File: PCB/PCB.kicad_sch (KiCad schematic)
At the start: 17 parts, among them J1 Conn_01x06_Female, J2 5054332681, U13 74HC165, U15 LT3042xMSE, U16 74HC165

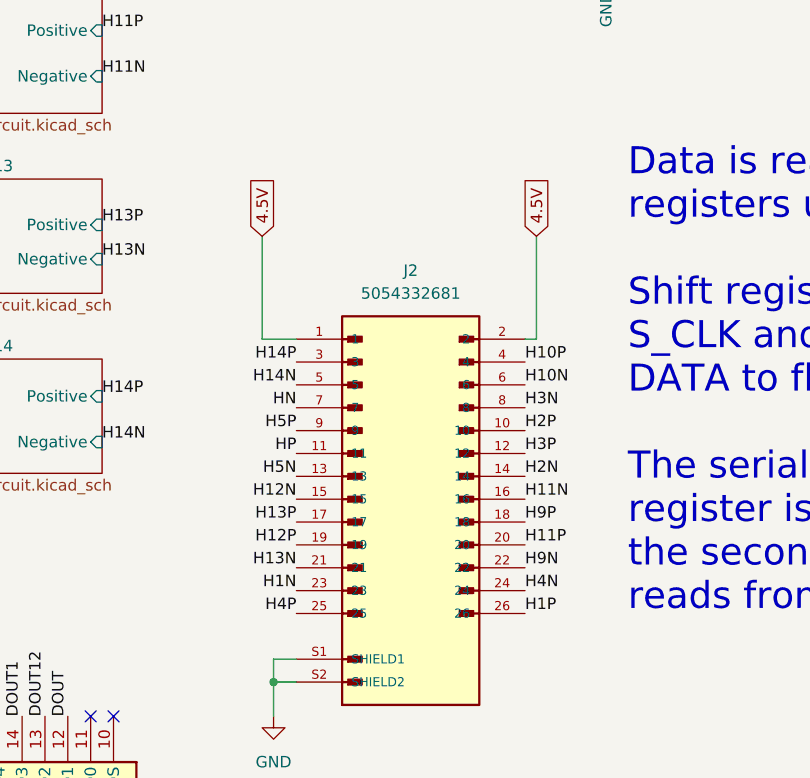
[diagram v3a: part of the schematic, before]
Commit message: New 75 by 75 mm
Dout has been traced, mostly on the same plane and have started on some of the required parts for the individual hx711 and will continue setting up sequential zones to reduce wires.
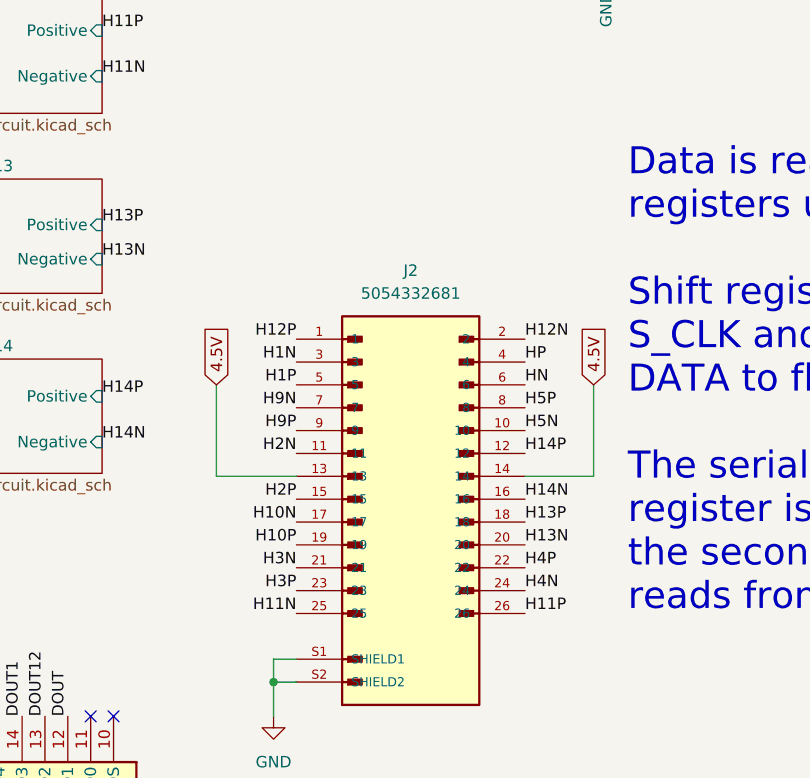
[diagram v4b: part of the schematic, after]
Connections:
- net 4.5V: now also J2.13, J2.14; no longer J2.1, J2.2
- net H10N: now also J2.17; no longer J2.6
- net H10P: now also J2.19; no longer J2.4
- net H11N: now also J2.25; no longer J2.16
- net H11P: now also J2.26; no longer J2.20
- net H12N: now also J2.2; no longer J2.15
- net H12P: now also J2.1; no longer J2.19
- net H13N: now also J2.20; no longer J2.21
- net H13P: now also J2.18; no longer J2.17
- net H14N: now also J2.16; no longer J2.5
- net H14P: now also J2.12; no longer J2.3
- net H1N: now also J2.3; no longer J2.23
- net H1P: now also J2.5; no longer J2.26
- net H2N: now also J2.11; no longer J2.14
- net H2P: now also J2.15; no longer J2.10
- net H3N: now also J2.21; no longer J2.8
- net H3P: now also J2.23; no longer J2.12
- net H4P: now also J2.22; no longer J2.25
- net H5N: now also J2.10; no longer J2.13
- net H5P: now also J2.8; no longer J2.9
- net H9N: now also J2.7; no longer J2.22
- net H9P: now also J2.9; no longer J2.18
- net HN: now also J2.6; no longer J2.7
- net HP: now also J2.4; no longer J2.11

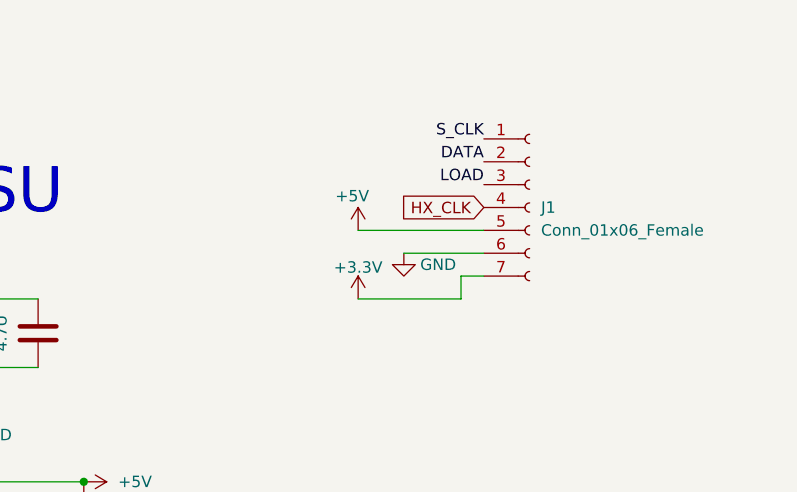
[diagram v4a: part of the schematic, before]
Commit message: Updated 7 pin header pinout
Pinout has been adjusted to match the pinout of the flight computer.
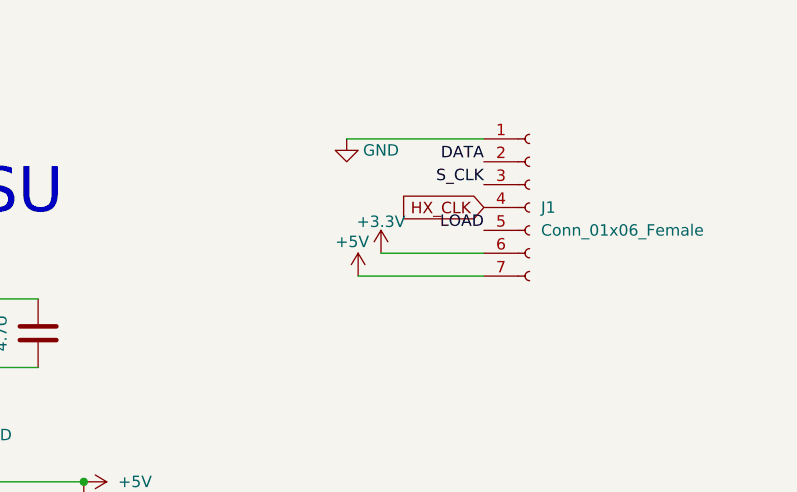
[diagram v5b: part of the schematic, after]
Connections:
- net +3.3V: now also J1.6 (Pin_6); no longer J1.7 (Pin_7)
- net +5V: now also J1.7 (Pin_7); no longer J1.5 (Pin_5)
- net GND: now also J1.1 (Pin_1); no longer J1.6 (Pin_6)
- net LOAD: now also J1.5 (Pin_5); no longer J1.3 (Pin_3)
- net S_CLK: now also J1.3 (Pin_3); no longer J1.1 (Pin_1)
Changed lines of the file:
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@@
 	(wire
 		(pts
-			(xy 251.46 41.91) (xy 248.92 41.91)
+			(xy 168.91 64.77) (xy 168.91 73.66)
 		)
 		(stroke
@@
 	(wire
 		(pts
-			(xy 168.91 64.77) (xy 168.91 73.66)
+			(xy 132.08 158.75) (xy 132.08 161.29)
 		)
 		(stroke
@@
 	(wire
 		(pts
-			(xy 132.08 158.75) (xy 132.08 161.29)
+			(xy 262.89 73.66) (xy 255.27 73.66)
 		)
 		(stroke
@@
 	(wire
 		(pts
-			(xy 262.89 73.66) (xy 255.27 73.66)
+			(xy 73.66 165.1) (xy 73.66 177.8)
 		)
 		(stroke
@@
 	(wire
 		(pts
-			(xy 73.66 165.1) (xy 73.66 177.8)
+			(xy 237.49 41.91) (xy 251.46 41.91)
 		)
 		(stroke
@@
 	(wire
 		(pts
-			(xy 242.57 39.37) (xy 251.46 39.37)
-		)
-		(stroke
-			(width 0)
-			(type default)
-		)
-	)
-	(wire
-		(pts
-			(xy 248.92 41.91) (xy 248.92 44.45)
-		)
-		(stroke
-			(width 0)
-			(type default)
-		)
-	)
-	(wire
-		(pts
 			(xy 27.94 165.1) (xy 20.32 165.1)
 		)
@@
 	(wire
 		(pts
-			(xy 20.32 180.34) (xy 20.32 177.8)
+			(xy 240.03 39.37) (xy 251.46 39.37)
 		)
 		(stroke
@@
 	(wire
 		(pts
-			(xy 237.49 36.83) (xy 251.46 36.83)
+			(xy 20.32 180.34) (xy 20.32 177.8)
 		)
 		(stroke
@@
 	(wire
 		(pts
-			(xy 191.77 52.07) (xy 201.93 52.07)
+			(xy 236.22 26.67) (xy 251.46 26.67)
 		)
 		(stroke
@@
 	(wire
 		(pts
-			(xy 132.08 165.1) (xy 132.08 161.29)
+			(xy 191.77 52.07) (xy 201.93 52.07)
 		)
 		(stroke
@@
 	(wire
 		(pts
-			(xy 114.3 190.5) (xy 114.3 193.04)
+			(xy 132.08 165.1) (xy 132.08 161.29)
 		)
 		(stroke
@@
 	(wire
 		(pts
-			(xy 160.02 64.77) (xy 160.02 68.58)
+			(xy 114.3 190.5) (xy 114.3 193.04)
 		)
 		(stroke
@@
 	(wire
 		(pts
-			(xy 171.45 62.23) (xy 168.91 62.23)
+			(xy 160.02 64.77) (xy 160.02 68.58)
 		)
 		(stroke
@@
 	(wire
 		(pts
-			(xy 248.92 44.45) (xy 237.49 44.45)
+			(xy 171.45 62.23) (xy 168.91 62.23)
 		)
 		(stroke
@@
 		)
 	)
-	(label "LOAD"
-		(at 251.46 31.75 180)
-		(fields_autoplaced yes)
-		(effects
-			(font
-				(size 1.27 1.27)
-			)
-			(justify right bottom)
-		)
-	)
 	(label "H5P"
 		(at 160.02 130.81 0)
@@
 		)
 	)
-	(label "S_CLK"
-		(at 251.46 26.67 180)
-		(fields_autoplaced yes)
-		(effects
-			(font
-				(size 1.27 1.27)
-			)
-			(justify right bottom)
-		)
-	)
 	(label "H3N"
 		(at 134.62 148.59 180)
@@
 		)
 	)
+	(label "LOAD"
+		(at 251.46 36.83 180)
+		(fields_autoplaced yes)
+		(effects
+			(font
+				(size 1.27 1.27)
+			)
+			(justify right bottom)
+		)
+	)
 	(label "H9P"
 		(at 134.62 133.35 180)
@@
 		)
 	)
+	(label "S_CLK"
+		(at 251.46 31.75 180)
+		(fields_autoplaced yes)
+		(effects
+			(font
+				(size 1.27 1.27)
+			)
+			(justify right bottom)
+		)
+	)
 	(label "H3P"
 		(at 134.62 151.13 180)
@@
 	)
 	(symbol
-		(lib_id "power:GND")
-		(at 242.57 39.37 0)
+		(lib_id "power:PWR_FLAG")
+		(at 257.81 116.84 0)
 		(unit 1)
 		(exclude_from_sim no)
@@
 		(on_board yes)
 		(dnp no)
-		(property "Reference" "#PWR015"
-			(at 242.57 45.72 0)
+		(property "Reference" "#FLG01"
+			(at 257.81 114.935 0)
 			(effects
 				(font
@@
 			)
 		)
-		(property "Value" "GND"
-			(at 246.38 40.64 0)
+		(property "Value" "PWR_FLAG"
+			(at 255.27 119.38 90)
 			(effects
 				(font
@@
 		)
 		(property "Footprint" ""
-			(at 242.57 39.37 0)
+			(at 257.81 116.84 0)
 			(effects
 				(font
@@
 			)
 		)
-		(property "Datasheet" ""
-			(at 242.57 39.37 0)
+		(property "Datasheet" "~"
+			(at 257.81 116.84 0)
 			(effects
 				(font
@@
 		)
 		(property "Description" ""
-			(at 242.57 39.37 0)
+			(at 257.81 116.84 0)
 			(effects
 				(font
@@
 			(project "PCB"
 				(path "/b6270a28-e0d9-4655-a18a-03dbf007b940"
-					(reference "#PWR015")
+					(reference "#FLG01")
 					(unit 1)
 				)
@@
 	)
 	(symbol
-		(lib_id "power:PWR_FLAG")
-		(at 257.81 116.84 0)
+		(lib_id "PCB-rescue:+5V-power")
+		(at 237.49 41.91 0)
 		(unit 1)
 		(exclude_from_sim no)
@@
 		(on_board yes)
 		(dnp no)
-		(property "Reference" "#FLG01"
-			(at 257.81 114.935 0)
+		(property "Reference" "#PWR014"
+			(at 237.49 45.72 0)
 			(effects
 				(font
@@
 			)
 		)
-		(property "Value" "PWR_FLAG"
-			(at 255.27 119.38 90)
+		(property "Value" "+5V"
+			(at 234.95 38.1 0)
 			(effects
 				(font
 					(size 1.27 1.27)
 				)
+				(justify left)
 			)
 		)
 		(property "Footprint" ""
-			(at 257.81 116.84 0)
+			(at 237.49 41.91 0)
 			(effects
 				(font
@@
 			)
 		)
-		(property "Datasheet" "~"
-			(at 257.81 116.84 0)
+		(property "Datasheet" ""
+			(at 237.49 41.91 0)
 			(effects
 				(font
@@
 		)
 		(property "Description" ""
-			(at 257.81 116.84 0)
+			(at 237.49 41.91 0)
 			(effects
 				(font
@@
 			(project "PCB"
 				(path "/b6270a28-e0d9-4655-a18a-03dbf007b940"
-					(reference "#FLG01")
+					(reference "#PWR014")
 					(unit 1)
 				)
@@
 	)
 	(symbol
+		(lib_id "power:GND")
+		(at 236.22 26.67 0)
+		(unit 1)
+		(exclude_from_sim no)
+		(in_bom yes)
+		(on_board yes)
+		(dnp no)
+		(property "Reference" "#PWR015"
+			(at 236.22 33.02 0)
+			(effects
+				(font
+					(size 1.27 1.27)
+				)
+				(hide yes)
+			)
+		)
+		(property "Value" "GND"
+			(at 240.03 27.94 0)
+			(effects
+				(font
+					(size 1.27 1.27)
+				)
+			)
+		)
+		(property "Footprint" ""
+			(at 236.22 26.67 0)
+			(effects
+				(font
+					(size 1.27 1.27)
+				)
+				(hide yes)
+			)
+		)
+		(property "Datasheet" ""
+			(at 236.22 26.67 0)
+			(effects
+				(font
+					(size 1.27 1.27)
+				)
+				(hide yes)
+			)
+		)
+		(property "Description" ""
+			(at 236.22 26.67 0)
+			(effects
+				(font
+					(size 1.27 1.27)
+				)
+				(hide yes)
+			)
+		)
+		(pin "1"
+		)
+		(instances
+			(project "PCB"
+				(path "/b6270a28-e0d9-4655-a18a-03dbf007b940"
+					(reference "#PWR015")
+					(unit 1)
+				)
+			)
+		)
+	)
+	(symbol
 		(lib_id "power:+3.3V")
 		(at 273.05 118.11 0)
@@
 	(symbol
 		(lib_id "power:+3.3V")
-		(at 237.49 44.45 0)
+		(at 240.03 39.37 0)
 		(unit 1)
 		(exclude_from_sim no)
@@
 		(fields_autoplaced yes)
 		(property "Reference" "#PWR01"
-			(at 237.49 48.26 0)
+			(at 240.03 43.18 0)
 			(effects
 				(font
@@
 		)
 		(property "Value" "+3.3V"
-			(at 237.49 40.9481 0)
+			(at 240.03 35.8681 0)
 			(effects
 				(font
@@
 		)
 		(property "Footprint" ""
-			(at 237.49 44.45 0)
+			(at 240.03 39.37 0)
 			(effects
 				(font
@@
 		)
 		(property "Datasheet" ""
-			(at 237.49 44.45 0)
+			(at 240.03 39.37 0)
 			(effects
 				(font
@@
 		)
 		(property "Description" ""
-			(at 237.49 44.45 0)
+			(at 240.03 39.37 0)
 			(effects
 				(font
@@
 					(unit 1)
 				)
-			)
-		)
-	)
-	(symbol
-		(lib_id "PCB-rescue:+5V-power")
-		(at 237.49 36.83 0)
-		(unit 1)
-		(exclude_from_sim no)
-		(in_bom yes)
-		(on_board yes)
-		(dnp no)
-		(property "Reference" "#PWR014"
-			(at 237.49 40.64 0)
-			(effects
-				(font
-					(size 1.27 1.27)
-				)
-				(hide yes)
-			)
-		)
-		(property "Value" "+5V"
-			(at 234.95 33.02 0)
-			(effects
-				(font
-					(size 1.27 1.27)
-				)
-				(justify left)
-			)
-		)
-		(property "Footprint" ""
-			(at 237.49 36.83 0)
-			(effects
-				(font
-					(size 1.27 1.27)
-				)
-				(hide yes)
-			)
-		)
-		(property "Datasheet" ""
-			(at 237.49 36.83 0)
-			(effects
-				(font
-					(size 1.27 1.27)
-				)
-				(hide yes)
-			)
-		)
-		(property "Description" ""
-			(at 237.49 36.83 0)
-			(effects
-				(font
-					(size 1.27 1.27)
-				)
-				(hide yes)
-			)
-		)
-		(pin "1"
-		)
-		(instances
-			(project "PCB"
-				(path "/b6270a28-e0d9-4655-a18a-03dbf007b940"
-					(reference "#PWR014")
-					(unit 1)
-				)

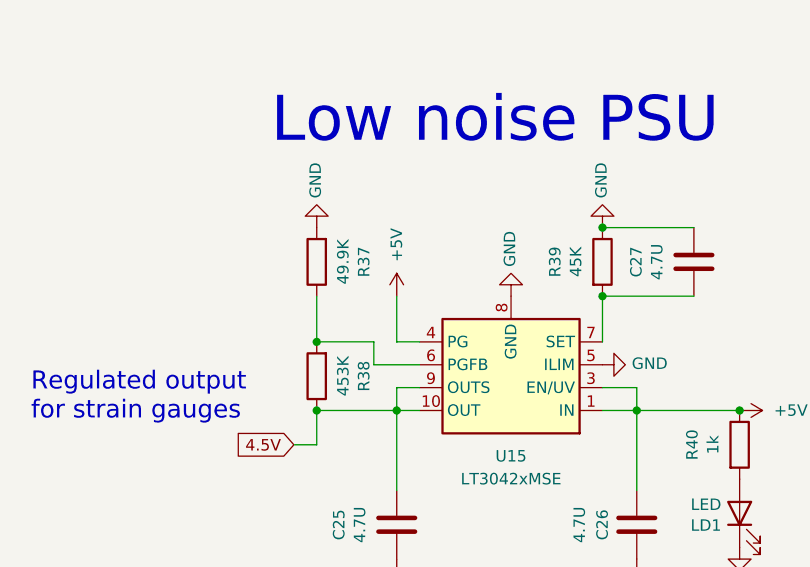
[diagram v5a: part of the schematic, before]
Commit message: Board updated for linear regulator and fills
Fills around each of the hx711 capacitor assemblies were changed to solid fills and the layout around the linear regulator was optimized to better fit with the data sheet.
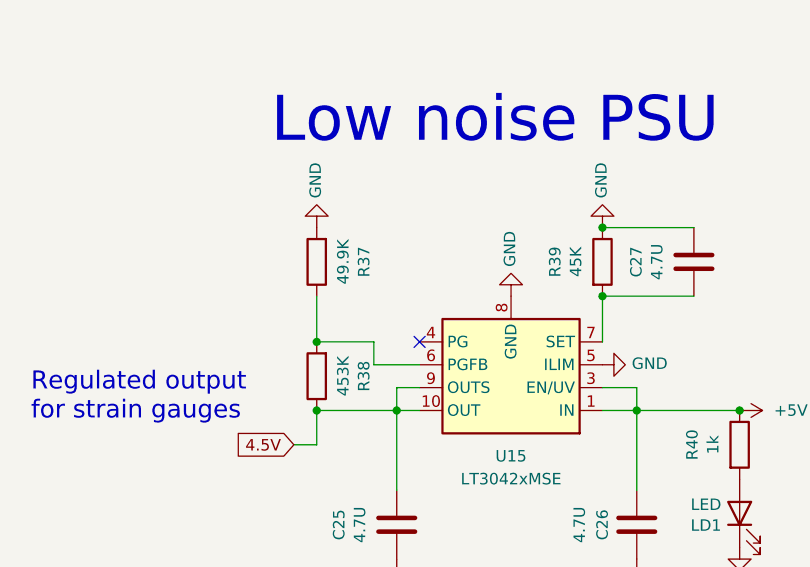
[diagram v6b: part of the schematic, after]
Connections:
- net +5V: no longer U15.4 (PG)
- no-connect marks 7 -> 8
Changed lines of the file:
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@@
 	)
 	(no_connect
+		(at 171.45 57.15)
+	)
+	(no_connect
 		(at 111.76 165.1)
 	)
@@
 	(wire
 		(pts
-			(xy 168.91 57.15) (xy 168.91 52.07)
-		)
-		(stroke
-			(width 0)
-			(type default)
-		)
-	)
-	(wire
-		(pts
 			(xy 157.48 68.58) (xy 160.02 68.58)
 		)
@@
 	(wire
 		(pts
-			(xy 171.45 57.15) (xy 168.91 57.15)
-		)
-		(stroke
-			(width 0)
-			(type default)
-		)
-	)
-	(wire
-		(pts
 			(xy 262.89 83.82) (xy 265.43 83.82)
 		)
@@
 					(unit 1)
 				)
-			)
-		)
-	)
-	(symbol
-		(lib_id "PCB-rescue:+5V-power")
-		(at 168.91 52.07 0)
-		(unit 1)
-		(exclude_from_sim no)
-		(in_bom yes)
-		(on_board yes)
-		(dnp no)
-		(property "Reference" "#PWR06"
-			(at 168.91 55.88 0)
-			(effects
-				(font
-					(size 1.27 1.27)
-				)
-				(hide yes)
-			)
-		)
-		(property "Value" "+5V"
-			(at 168.91 48.26 90)
-			(effects
-				(font
-					(size 1.27 1.27)
-				)
-				(justify left)
-			)
-		)
-		(property "Footprint" ""
-			(at 168.91 52.07 0)
-			(effects
-				(font
-					(size 1.27 1.27)
-				)
-				(hide yes)
-			)
-		)
-		(property "Datasheet" ""
-			(at 168.91 52.07 0)
-			(effects
-				(font
-					(size 1.27 1.27)
-				)
-				(hide yes)
-			)
-		)
-		(property "Description" ""
-			(at 168.91 52.07 0)
-			(effects
-				(font
-					(size 1.27 1.27)
-				)
-				(hide yes)
-			)
-		)
-		(pin "1"
-		)
-		(instances
-			(project "PCB"
-				(path "/b6270a28-e0d9-4655-a18a-03dbf007b940"
-					(reference "#PWR06")
-					(unit 1)
-				)
